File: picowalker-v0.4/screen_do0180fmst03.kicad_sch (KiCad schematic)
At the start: 0 parts

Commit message: v0.4: schematic laid out first draft
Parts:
- added C35: 10u, Capacitor_SMD:C_0603_1608Metric, symbol Device:C
- added C36: 4.7u, Capacitor_SMD:C_0402_1005Metric, symbol Device:C
- added U7: DO0180FMST0x, symbol picowalker:DO0180FMST0x
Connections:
- new net +3.3V: C36.2, U7.17 (IM1), U7.24 (VCI), U7.26 (VDDIO)
- new net GND: C35.2, C36.1, U7.19 (IM0), U7.21 (GND), U7.23 (MIPI_CLKP), U7.25 (MIPI_CLKN), U7.27 (GND), U7.28 (GND), U7.29 (MIPI_D0P), U7.3 (DCX_RS), U7.31 (MIPI_D0N), U7.33 (GND), U7.4 (GND)
- new net PWR_EN: U7.22 (PWR_EN)
- new net SCK: U7.9 (SCK)
- new net SCL: U7.8 (TP_SCL)
- new net SD0: U7.5 (SD0/SDI)
- new net SD1: U7.7 (SD1/SDO)
- new net SD2: U7.13 (SD2)
- new net SD3: U7.15 (SD3)
- new net SDA: U7.10 (TP_SDA)
- new net TP_INT: U7.12 (TP_INT)
- new net TP_RESET: U7.14 (TP_RESET)
- new net VSYS: C35.1, U7.18 (VBAT), U7.20 (VBAT)
- new net ~{CS}: U7.11 (~{CS})
- new net ~{RST}: U7.1 (~{RESET})
- no-connect marks 0 -> 2

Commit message: v0.4: more rationalisation
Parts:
- C35: value 10u -> 4.7u; footprint Capacitor_SMD:C_0603_1608Metric -> Capacitor_SMD:C_0402_1005Metric
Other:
- note added: "IM0/IM1 low/high = QSPI mode"
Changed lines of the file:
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@@
 		(members "PWR_EN" "~{RST}")
+	)
+	(text "IM0/IM1 low/high = QSPI mode"
+		(exclude_from_sim no)
+		(at 74.422 112.268 0)
+		(effects
+			(font
+				(size 1.27 1.27)
+			)
+			(justify left)
+		)
 	)
 	(text_box "Decoupling and bulk"
@@
 			)
 		)
-		(property "Value" "10u"
+		(property "Value" "4.7u"
 			(at 30.48 39.3699 0)
 			(effects
@@
 			)
 		)
-		(property "Footprint" "Capacitor_SMD:C_0603_1608Metric"
+		(property "Footprint" "Capacitor_SMD:C_0402_1005Metric"
 			(at 35.2552 41.91 0)
 			(effects

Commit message: v0.4: first rough placement of PCB
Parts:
- U7: footprint (none) -> picowalker:AXE534127
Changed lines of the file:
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@@
 			)
 		)
-		(property "Footprint" ""
+		(property "Footprint" "picowalker:AXE534127"
 			(at 139.7 55.88 0)
 			(effects

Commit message: v0.4: good start on routing
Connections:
- net TP_VCC: now reaches U7.16 (TP_VCC)
- net TE: now reaches U7.2 (TE)
- net PWR_EN renamed AUX.PWR_EN
- net SCK renamed QSPI.SCK
- net SCL renamed TP_I2C.SCL
- net SD0 renamed QSPI.SD0
- net SD1 renamed QSPI.SD1
- net SD2 renamed QSPI.SD2
- net SD3 renamed QSPI.SD3
- net SDA renamed TP_I2C.SDA
- net ~{RST} renamed AUX.~{RST}
- no-connect marks 2 -> 1
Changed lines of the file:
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@@
 	)
 	(no_connect
-		(at 160.02 68.58)
-	)
-	(no_connect
-		(at 144.78 52.07)
+		(at 144.78 48.26)
 	)
 	(bus_entry
@@
 	)
 	(bus_entry
-		(at 105.41 97.79)
+		(at 101.6 97.79)
 		(size 2.54 2.54)
 		(stroke
@@
 	)
 	(bus_entry
-		(at 105.41 95.25)
+		(at 101.6 95.25)
 		(size 2.54 2.54)
 		(stroke
@@
 		)
 	)
+	(wire
+		(pts
+			(xy 156.21 97.79) (xy 167.64 97.79)
+		)
+		(stroke
+			(width 0)
+			(type default)
+		)
+	)
 	(bus
 		(pts
@@
 	(wire
 		(pts
+			(xy 156.21 68.58) (xy 163.83 68.58)
+		)
+		(stroke
+			(width 0)
+			(type default)
+		)
+	)
+	(wire
+		(pts
 			(xy 109.22 81.28) (xy 123.19 81.28)
 		)
@@
 	(wire
 		(pts
-			(xy 107.95 100.33) (xy 123.19 100.33)
+			(xy 104.14 100.33) (xy 123.19 100.33)
 		)
 		(stroke
@@
 	(wire
 		(pts
-			(xy 123.19 102.87) (xy 105.41 102.87)
+			(xy 105.41 102.87) (xy 123.19 102.87)
 		)
 		(stroke
@@
 	(bus
 		(pts
-			(xy 105.41 95.25) (xy 105.41 97.79)
+			(xy 101.6 95.25) (xy 101.6 97.79)
 		)
 		(stroke
@@
 	(wire
 		(pts
-			(xy 156.21 97.79) (xy 160.02 97.79)
-		)
-		(stroke
-			(width 0)
-			(type default)
-		)
-	)
-	(wire
-		(pts
 			(xy 134.62 46.99) (xy 134.62 55.88)
 		)
@@
 	(wire
 		(pts
-			(xy 144.78 52.07) (xy 144.78 55.88)
+			(xy 144.78 48.26) (xy 144.78 55.88)
 		)
 		(stroke
@@
 	(wire
 		(pts
-			(xy 156.21 68.58) (xy 160.02 68.58)
-		)
-		(stroke
-			(width 0)
-			(type default)
-		)
-	)
-	(wire
-		(pts
 			(xy 34.29 30.48) (xy 34.29 34.29)
 		)
@@
 	(wire
 		(pts
-			(xy 107.95 97.79) (xy 123.19 97.79)
-		)
-		(stroke
-			(width 0)
-			(type default)
-		)
-	)
-	(label "SCL"
-		(at 113.03 97.79 0)
-		(effects
-			(font
-				(size 1.27 1.27)
-			)
-			(justify left bottom)
-		)
-	)
-	(label "SDA"
-		(at 113.03 100.33 0)
-		(effects
-			(font
-				(size 1.27 1.27)
-			)
-			(justify left bottom)
-		)
-	)
-	(label "~{RST}"
-		(at 113.03 71.12 0)
-		(effects
-			(font
-				(size 1.27 1.27)
-			)
-			(justify left bottom)
-		)
-	)
-	(label "SD1"
-		(at 115.57 81.28 0)
-		(effects
-			(font
-				(size 1.27 1.27)
-			)
-			(justify left bottom)
-		)
-	)
-	(label "SD2"
-		(at 115.57 83.82 0)
-		(effects
-			(font
-				(size 1.27 1.27)
-			)
-			(justify left bottom)
-		)
-	)
-	(label "SD0"
-		(at 115.57 78.74 0)
-		(effects
-			(font
-				(size 1.27 1.27)
-			)
-			(justify left bottom)
-		)
-	)
-	(label "SCK"
-		(at 115.57 76.2 0)
-		(effects
-			(font
-				(size 1.27 1.27)
-			)
-			(justify left bottom)
-		)
-	)
-	(label "SD3"
-		(at 115.57 86.36 0)
-		(effects
-			(font
-				(size 1.27 1.27)
-			)
-			(justify left bottom)
-		)
-	)
-	(label "PWR_EN"
+			(xy 104.14 97.79) (xy 123.19 97.79)
+		)
+		(stroke
+			(width 0)
+			(type default)
+		)
+	)
+	(label "TP_I2C.SCL"
+		(at 106.68 97.79 0)
+		(effects
+			(font
+				(size 1.27 1.27)
+			)
+			(justify left bottom)
+		)
+	)
+	(label "TP_I2C.SDA"
+		(at 106.68 100.33 0)
+		(effects
+			(font
+				(size 1.27 1.27)
+			)
+			(justify left bottom)
+		)
+	)
+	(label "TP_VCC"
+		(at 144.78 53.34 0)
+		(effects
+			(font
+				(size 1.27 1.27)
+			)
+			(justify left bottom)
+		)
+	)
+	(label "AUX.~{RST}"
+		(at 110.49 71.12 0)
+		(effects
+			(font
+				(size 1.27 1.27)
+			)
+			(justify left bottom)
+		)
+	)
+	(label "TP_INT"
+		(at 158.75 97.79 0)
+		(effects
+			(font
+				(size 1.27 1.27)
+			)
+			(justify left bottom)
+		)
+	)
+	(label "QSPI.SD1"
+		(at 113.03 81.28 0)
+		(effects
+			(font
+				(size 1.27 1.27)
+			)
+			(justify left bottom)
+		)
+	)
+	(label "QSPI.SD2"
+		(at 113.03 83.82 0)
+		(effects
+			(font
+				(size 1.27 1.27)
+			)
+			(justify left bottom)
+		)
+	)
+	(label "QSPI.SD0"
+		(at 113.03 78.74 0)
+		(effects
+			(font
+				(size 1.27 1.27)
+			)
+			(justify left bottom)
+		)
+	)
+	(label "QSPI.SCK"
+		(at 113.03 76.2 0)
+		(effects
+			(font
+				(size 1.27 1.27)
+			)
+			(justify left bottom)
+		)
+	)
+	(label "TP_RESET"
+		(at 106.68 102.87 0)
+		(effects
+			(font
+				(size 1.27 1.27)
+			)
+			(justify left bottom)
+		)
+	)
+	(label "QSPI.SD3"
+		(at 113.03 86.36 0)
+		(effects
+			(font
+				(size 1.27 1.27)
+			)
+			(justify left bottom)
+		)
+	)
+	(label "AUX.PWR_EN"
 		(at 110.49 68.58 0)
 		(effects
@@
 	(hierarchical_label "TP_INT"
 		(shape output)
-		(at 160.02 97.79 0)
+		(at 167.64 97.79 0)
+		(effects
+			(font
+				(size 1.27 1.27)
+			)
+			(justify left)
+		)
+	)
+	(hierarchical_label "TE"
+		(shape output)
+		(at 163.83 68.58 0)
 		(effects
 			(font
@@
 	(hierarchical_label "TP_I2C{I2C}"
 		(shape input)
-		(at 105.41 95.25 180)
-		(effects
-			(font
+		(at 101.6 95.25 180)
+		(effects
+			(font

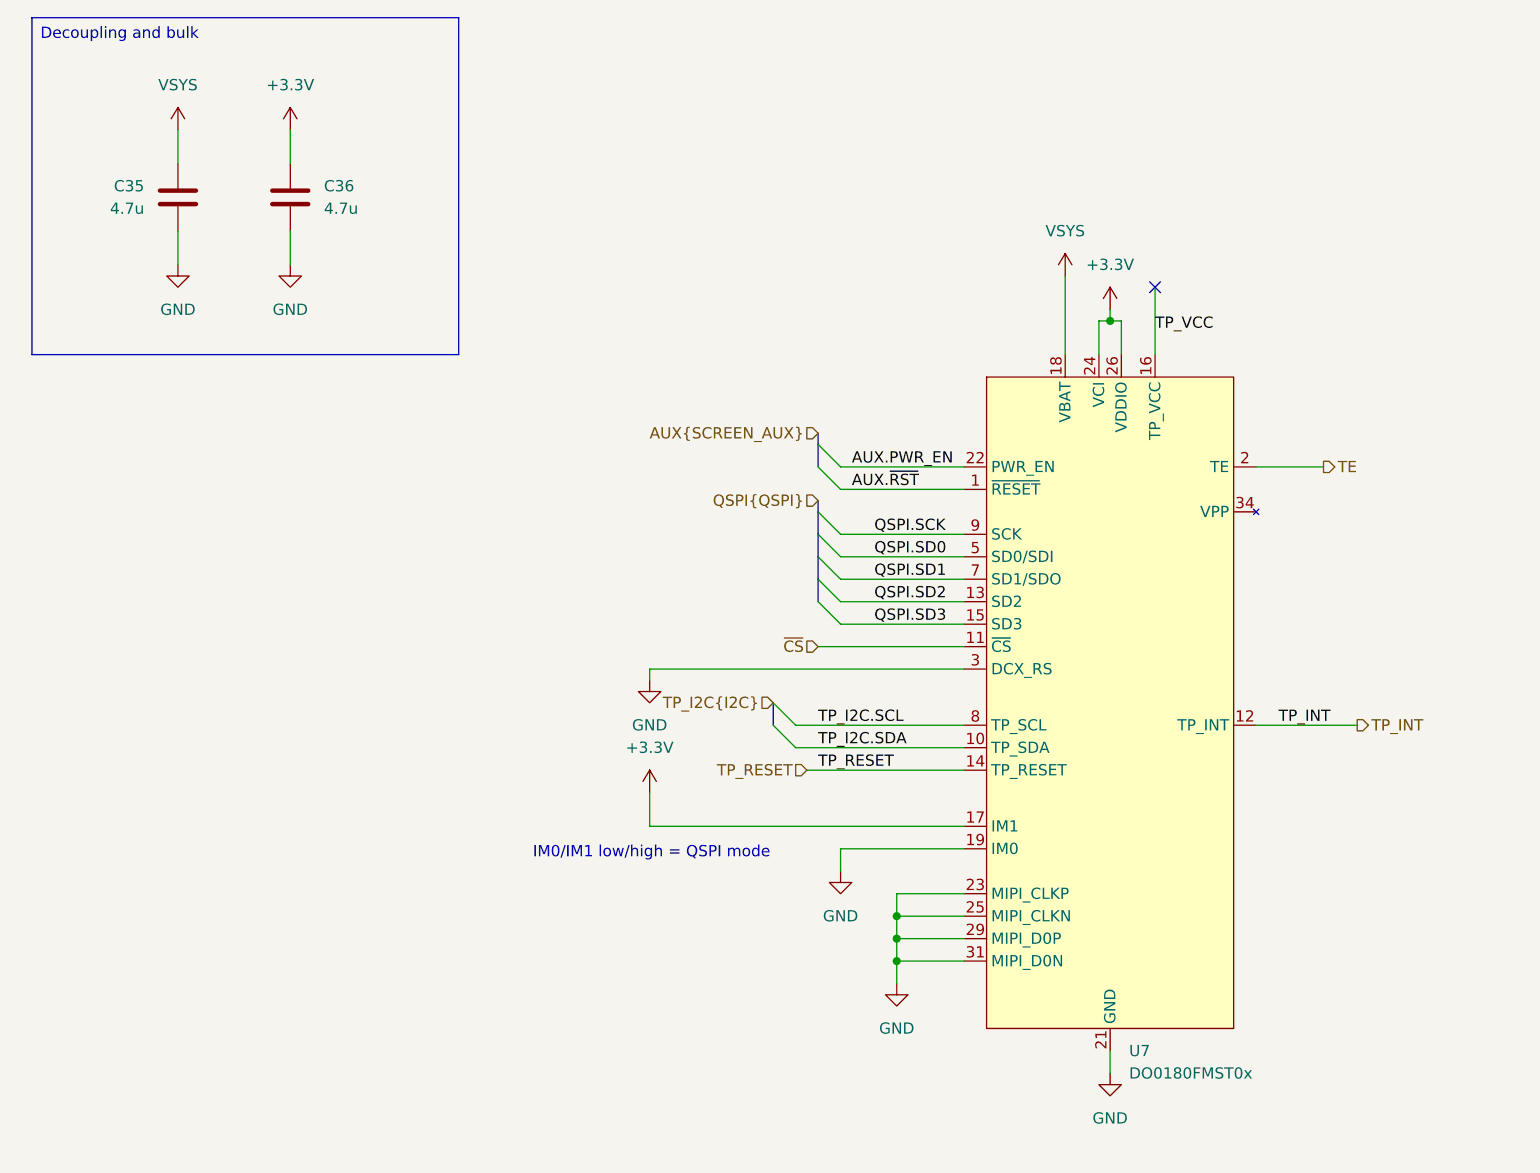
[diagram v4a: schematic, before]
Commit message: v0.4: add test points for touch pad
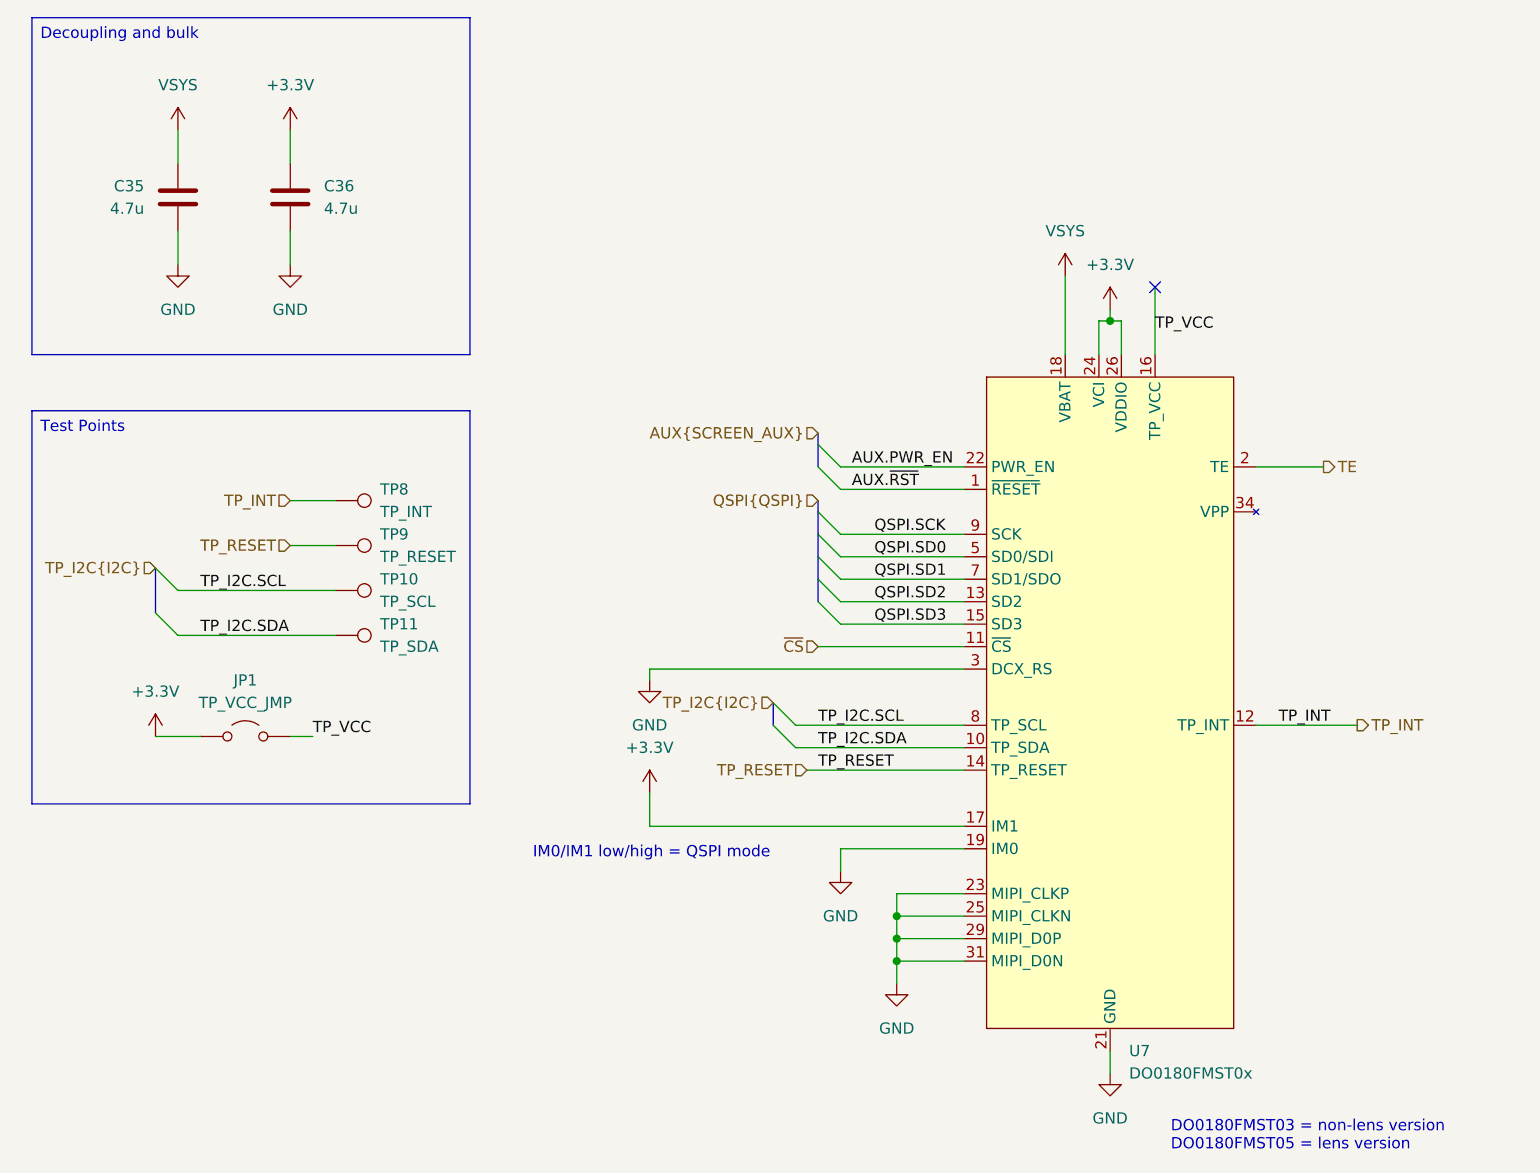
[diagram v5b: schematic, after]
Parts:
- added JP1: TP_VCC_JMP, Jumper:SolderJumper-2_P1.3mm_Open_RoundedPad1.0x1.5mm, symbol Jumper:Jumper_2_Open
- added TP10: TP_SCL, picowalker:TestPoint_Pad_D1.0mm_Nosilk, symbol Connector:TestPoint
- added TP11: TP_SDA, picowalker:TestPoint_Pad_D1.0mm_Nosilk, symbol Connector:TestPoint
- added TP8: TP_INT, picowalker:TestPoint_Pad_D1.0mm_Nosilk, symbol Connector:TestPoint
- added TP9: TP_RESET, picowalker:TestPoint_Pad_D1.0mm_Nosilk, symbol Connector:TestPoint
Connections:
- net +3.3V: now also JP1.1 (A)
- net TP_I2C.SCL: now also TP10.1
- net TP_I2C.SDA: now also TP11.1
- net TP_INT: now also TP8.1
- net TP_RESET: now also TP9.1
- net TP_VCC: now also JP1.2 (B)
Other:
- note added: "DO0180FMST03 = non-lens version DO0180FMST05 = lens version"

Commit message: v0.4: connect i2c to TP and add silkscreen labels
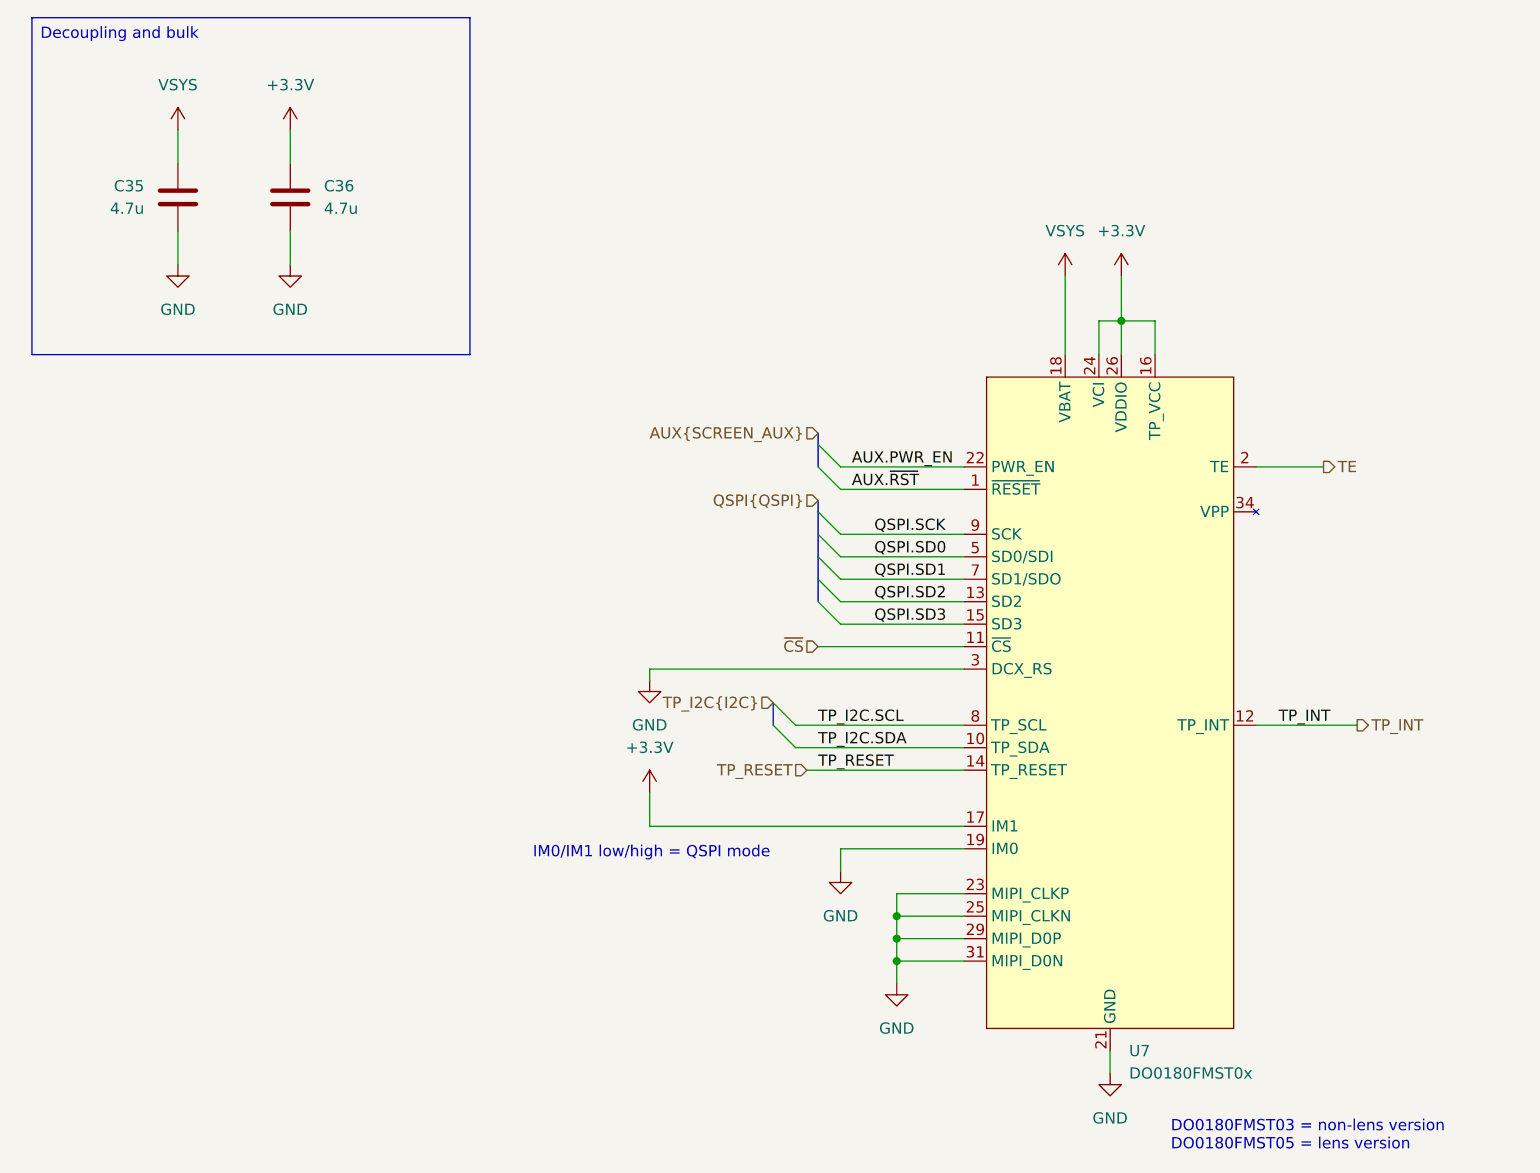
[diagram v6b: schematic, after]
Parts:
- removed JP1: TP_VCC_JMP, Jumper:SolderJumper-2_P1.3mm_Open_RoundedPad1.0x1.5mm, symbol Jumper:Jumper_2_Open
- removed TP10: TP_SCL, picowalker:TestPoint_Pad_D1.0mm_Nosilk, symbol Connector:TestPoint
- removed TP11: TP_SDA, picowalker:TestPoint_Pad_D1.0mm_Nosilk, symbol Connector:TestPoint
- removed TP8: TP_INT, picowalker:TestPoint_Pad_D1.0mm_Nosilk, symbol Connector:TestPoint
- removed TP9: TP_RESET, picowalker:TestPoint_Pad_D1.0mm_Nosilk, symbol Connector:TestPoint
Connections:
- net TP_VCC is gone; now on net +3.3V: U7.16 (TP_VCC)
- no-connect marks 1 -> 0
